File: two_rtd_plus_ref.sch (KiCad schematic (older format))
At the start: 19 parts, among them J3 4-wire RTD, J4 4-wire RTD, J5 Bypass 2nd RTD

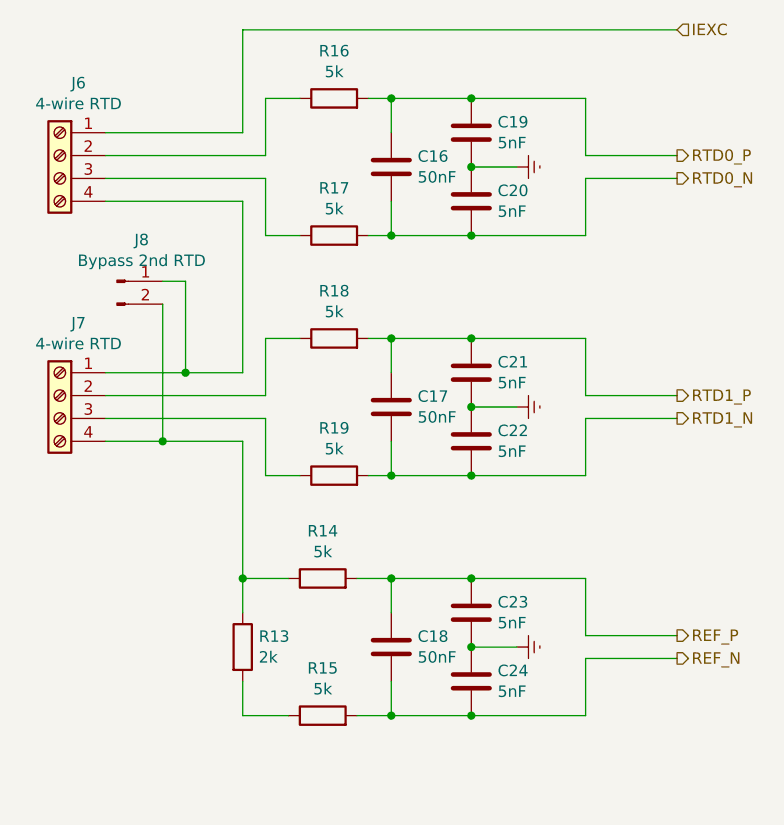
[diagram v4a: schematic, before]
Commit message: placed the components
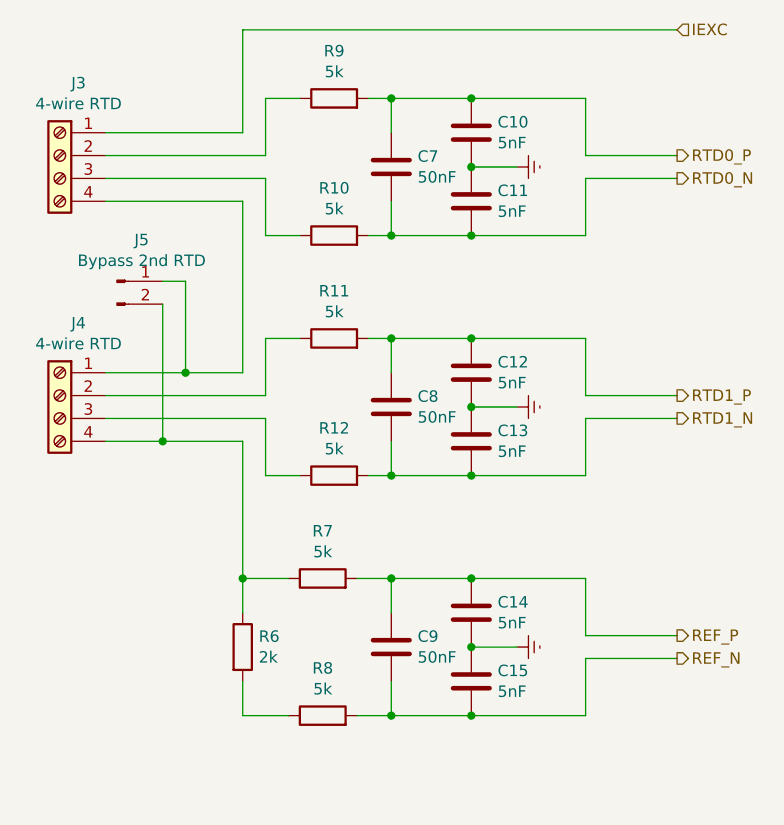
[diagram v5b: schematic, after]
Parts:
- J5: footprint (none) -> Connector_PinHeader_2.54mm:PinHeader_1x02_P2.54mm_Vertical
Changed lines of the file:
@@
 AR Path="/5EC374D6/5EC48F50" Ref="J3"  Part="1"
 AR Path="/5ED0B429/5EC48F50" Ref="J6"  Part="1"
-F 0 "J6" H 3568 2917 50  0000 C CNN
+F 0 "J3" H 3568 2917 50  0000 C CNN
 F 1 "4-wire RTD" H 3568 2826 50  0000 C CNN
 F 2 "temp4x4:screw_term_4x" H 3650 2600 50  0001 C CNN
@@
 AR Path="/5EC374D6/5EC48F56" Ref="C11"  Part="1"
 AR Path="/5ED0B429/5EC48F56" Ref="C20"  Part="1"
-F 0 "C20" H 5565 2846 50  0000 L CNN
+F 0 "C11" H 5565 2846 50  0000 L CNN
 F 1 "5nF" H 5565 2755 50  0000 L CNN
 F 2 "Capacitor_SMD:C_0805_2012Metric_Pad1.15x1.40mm_HandSolder" H 5488 2650 50  0001 C CNN
@@
 AR Path="/5EC374D6/5EC48F5C" Ref="C7"  Part="1"
 AR Path="/5ED0B429/5EC48F5C" Ref="C16"  Part="1"
-F 0 "C16" H 5215 2696 50  0000 L CNN
+F 0 "C7" H 5215 2696 50  0000 L CNN
 F 1 "50nF" H 5215 2605 50  0000 L CNN
 F 2 "Capacitor_SMD:C_0805_2012Metric_Pad1.15x1.40mm_HandSolder" H 5138 2500 50  0001 C CNN
@@
 AR Path="/5EC374D6/5EC48F62" Ref="C10"  Part="1"
 AR Path="/5ED0B429/5EC48F62" Ref="C19"  Part="1"
-F 0 "C19" H 5565 2546 50  0000 L CNN
+F 0 "C10" H 5565 2546 50  0000 L CNN
 F 1 "5nF" H 5565 2455 50  0000 L CNN
 F 2 "Capacitor_SMD:C_0805_2012Metric_Pad1.15x1.40mm_HandSolder" H 5488 2350 50  0001 C CNN
@@
 AR Path="/5EC374D6/5EC48F68" Ref="#PWR014"  Part="1"
 AR Path="/5ED0B429/5EC48F68" Ref="#PWR017"  Part="1"
-F 0 "#PWR017" H 5650 2400 50  0001 C CNN
+F 0 "#PWR014" H 5650 2400 50  0001 C CNN
 F 1 "Earth" H 5650 2500 50  0001 C CNN
 F 2 "" H 5650 2650 50  0001 C CNN
@@
 AR Path="/5EC374D6/5EC48F74" Ref="R9"  Part="1"
 AR Path="/5ED0B429/5EC48F74" Ref="R16"  Part="1"
-F 0 "R16" V 5057 2350 50  0000 C CNN
+F 0 "R9" V 5057 2350 50  0000 C CNN
 F 1 "5k" V 4966 2350 50  0000 C CNN
 F 2 "Resistor_SMD:R_0805_2012Metric_Pad1.15x1.40mm_HandSolder" V 4780 2350 50  0001 C CNN
@@
 AR Path="/5EC374D6/5EC48F7B" Ref="R10"  Part="1"
 AR Path="/5ED0B429/5EC48F7B" Ref="R17"  Part="1"
-F 0 "R17" V 5057 2950 50  0000 C CNN
+F 0 "R10" V 5057 2950 50  0000 C CNN
 F 1 "5k" V 4966 2950 50  0000 C CNN
 F 2 "Resistor_SMD:R_0805_2012Metric_Pad1.15x1.40mm_HandSolder" V 4780 2950 50  0001 C CNN
@@
 AR Path="/5EC374D6/5EC48F91" Ref="J4"  Part="1"
 AR Path="/5ED0B429/5EC48F91" Ref="J7"  Part="1"
-F 0 "J7" H 3568 3967 50  0000 C CNN
+F 0 "J4" H 3568 3967 50  0000 C CNN
 F 1 "4-wire RTD" H 3568 3876 50  0000 C CNN
 F 2 "temp4x4:screw_term_4x" H 3650 3650 50  0001 C CNN
@@
 AR Path="/5EC374D6/5EC48F97" Ref="C13"  Part="1"
 AR Path="/5ED0B429/5EC48F97" Ref="C22"  Part="1"
-F 0 "C22" H 5565 3896 50  0000 L CNN
+F 0 "C13" H 5565 3896 50  0000 L CNN
 F 1 "5nF" H 5565 3805 50  0000 L CNN
 F 2 "Capacitor_SMD:C_0805_2012Metric_Pad1.15x1.40mm_HandSolder" H 5488 3700 50  0001 C CNN
@@
 AR Path="/5EC374D6/5EC48F9D" Ref="C8"  Part="1"
 AR Path="/5ED0B429/5EC48F9D" Ref="C17"  Part="1"
-F 0 "C17" H 5215 3746 50  0000 L CNN
+F 0 "C8" H 5215 3746 50  0000 L CNN
 F 1 "50nF" H 5215 3655 50  0000 L CNN
 F 2 "Capacitor_SMD:C_0805_2012Metric_Pad1.15x1.40mm_HandSolder" H 5138 3550 50  0001 C CNN
@@
 AR Path="/5EC374D6/5EC48FA3" Ref="C12"  Part="1"
 AR Path="/5ED0B429/5EC48FA3" Ref="C21"  Part="1"
-F 0 "C21" H 5565 3596 50  0000 L CNN
+F 0 "C12" H 5565 3596 50  0000 L CNN
 F 1 "5nF" H 5565 3505 50  0000 L CNN
 F 2 "Capacitor_SMD:C_0805_2012Metric_Pad1.15x1.40mm_HandSolder" H 5488 3400 50  0001 C CNN
@@
 AR Path="/5EC374D6/5EC48FA9" Ref="#PWR015"  Part="1"
 AR Path="/5ED0B429/5EC48FA9" Ref="#PWR018"  Part="1"
-F 0 "#PWR018" H 5650 3450 50  0001 C CNN
+F 0 "#PWR015" H 5650 3450 50  0001 C CNN
 F 1 "Earth" H 5650 3550 50  0001 C CNN
 F 2 "" H 5650 3700 50  0001 C CNN
@@
 AR Path="/5EC374D6/5EC48FB5" Ref="R11"  Part="1"
 AR Path="/5ED0B429/5EC48FB5" Ref="R18"  Part="1"
-F 0 "R18" V 5057 3400 50  0000 C CNN
+F 0 "R11" V 5057 3400 50  0000 C CNN
 F 1 "5k" V 4966 3400 50  0000 C CNN
 F 2 "Resistor_SMD:R_0805_2012Metric_Pad1.15x1.40mm_HandSolder" V 4780 3400 50  0001 C CNN
@@
 AR Path="/5EC374D6/5EC48FBC" Ref="R12"  Part="1"
 AR Path="/5ED0B429/5EC48FBC" Ref="R19"  Part="1"
-F 0 "R19" V 5057 4000 50  0000 C CNN
+F 0 "R12" V 5057 4000 50  0000 C CNN
 F 1 "5k" V 4966 4000 50  0000 C CNN
 F 2 "Resistor_SMD:R_0805_2012Metric_Pad1.15x1.40mm_HandSolder" V 4780 4000 50  0001 C CNN
@@
 AR Path="/5EC374D6/5EC48FD1" Ref="C15"  Part="1"
 AR Path="/5ED0B429/5EC48FD1" Ref="C24"  Part="1"
-F 0 "C24" H 5565 4946 50  0000 L CNN
+F 0 "C15" H 5565 4946 50  0000 L CNN
 F 1 "5nF" H 5565 4855 50  0000 L CNN
 F 2 "Capacitor_SMD:C_0805_2012Metric_Pad1.15x1.40mm_HandSolder" H 5488 4750 50  0001 C CNN
@@
 AR Path="/5EC374D6/5EC48FD7" Ref="C9"  Part="1"
 AR Path="/5ED0B429/5EC48FD7" Ref="C18"  Part="1"
-F 0 "C18" H 5215 4796 50  0000 L CNN
+F 0 "C9" H 5215 4796 50  0000 L CNN
 F 1 "50nF" H 5215 4705 50  0000 L CNN
 F 2 "Capacitor_SMD:C_0805_2012Metric_Pad1.15x1.40mm_HandSolder" H 5138 4600 50  0001 C CNN
@@
 AR Path="/5EC374D6/5EC48FDD" Ref="C14"  Part="1"
 AR Path="/5ED0B429/5EC48FDD" Ref="C23"  Part="1"
-F 0 "C23" H 5565 4646 50  0000 L CNN
+F 0 "C14" H 5565 4646 50  0000 L CNN
 F 1 "5nF" H 5565 4555 50  0000 L CNN
 F 2 "Capacitor_SMD:C_0805_2012Metric_Pad1.15x1.40mm_HandSolder" H 5488 4450 50  0001 C CNN
@@
 AR Path="/5EC374D6/5EC48FE3" Ref="#PWR016"  Part="1"
 AR Path="/5ED0B429/5EC48FE3" Ref="#PWR019"  Part="1"
-F 0 "#PWR019" H 5650 4500 50  0001 C CNN
+F 0 "#PWR016" H 5650 4500 50  0001 C CNN
 F 1 "Earth" H 5650 4600 50  0001 C CNN
 F 2 "" H 5650 4750 50  0001 C CNN
@@
 AR Path="/5EC374D6/5EC48FEF" Ref="R7"  Part="1"
 AR Path="/5ED0B429/5EC48FEF" Ref="R14"  Part="1"
-F 0 "R14" V 5007 4450 50  0000 C CNN
+F 0 "R7" V 5007 4450 50  0000 C CNN
 F 1 "5k" V 4916 4450 50  0000 C CNN
 F 2 "Resistor_SMD:R_0805_2012Metric_Pad1.15x1.40mm_HandSolder" V 4730 4450 50  0001 C CNN
@@
 AR Path="/5EC374D6/5EC48FF6" Ref="R8"  Part="1"
 AR Path="/5ED0B429/5EC48FF6" Ref="R15"  Part="1"
-F 0 "R15" V 5007 5050 50  0000 C CNN
+F 0 "R8" V 5007 5050 50  0000 C CNN
 F 1 "5k" V 4916 5050 50  0000 C CNN
 F 2 "Resistor_SMD:R_0805_2012Metric_Pad1.15x1.40mm_HandSolder" V 4730 5050 50  0001 C CNN
@@
 AR Path="/5EC374D6/5EC49006" Ref="R6"  Part="1"
 AR Path="/5ED0B429/5EC49006" Ref="R13"  Part="1"
-F 0 "R13" H 4520 4796 50  0000 L CNN
+F 0 "R6" H 4520 4796 50  0000 L CNN
 F 1 "2k" H 4520 4705 50  0000 L CNN
 F 2 "Resistor_SMD:R_0805_2012Metric_Pad1.15x1.40mm_HandSolder" V 4380 4750 50  0001 C CNN
@@
 AR Path="/5EC374D6/5ECF80D6" Ref="J5"  Part="1"
 AR Path="/5ED0B429/5ECF80D6" Ref="J8"  Part="1"
-F 0 "J8" H 4008 3331 50  0000 C CNN
+F 0 "J5" H 4008 3331 50  0000 C CNN
 F 1 "Bypass 2nd RTD" H 4008 3240 50  0000 C CNN
-F 2 "" H 3900 3150 50  0001 C CNN
+F 2 "Connector_PinHeader_2.54mm:PinHeader_1x02_P2.54mm_Vertical" H 3900 3150 50  0001 C CNN
 F 3 "~" H 3900 3150 50  0001 C CNN
 	1    3900 3150

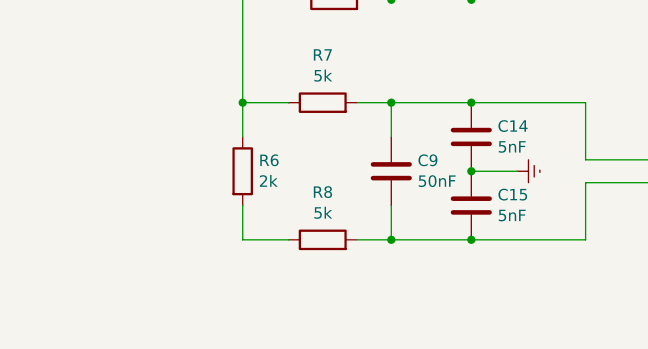
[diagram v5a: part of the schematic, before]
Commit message: changed pin connections to simplify the layout
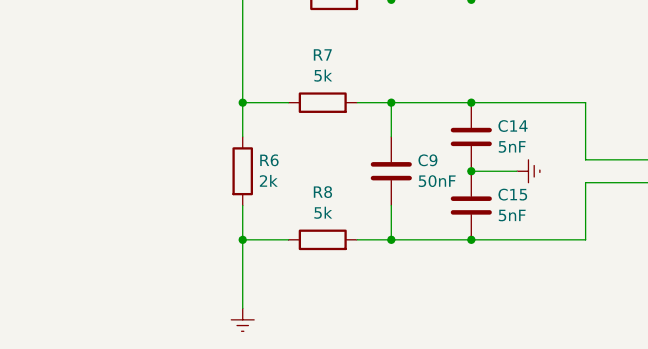
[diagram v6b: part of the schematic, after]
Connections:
- net Earth: now also R6.2, R8.1
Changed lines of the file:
@@
 AR Path="/5EC374D6/5EC48F68" Ref="#PWR014"  Part="1"
 AR Path="/5ED0B429/5EC48F68" Ref="#PWR017"  Part="1"
-F 0 "#PWR014" H 5650 2400 50  0001 C CNN
+F 0 "#PWR017" H 5650 2400 50  0001 C CNN
 F 1 "Earth" H 5650 2500 50  0001 C CNN
 F 2 "" H 5650 2650 50  0001 C CNN
@@
 AR Path="/5EC374D6/5EC48FA9" Ref="#PWR015"  Part="1"
 AR Path="/5ED0B429/5EC48FA9" Ref="#PWR018"  Part="1"
-F 0 "#PWR015" H 5650 3450 50  0001 C CNN
+F 0 "#PWR018" H 5650 3450 50  0001 C CNN
 F 1 "Earth" H 5650 3550 50  0001 C CNN
 F 2 "" H 5650 3700 50  0001 C CNN
@@
 AR Path="/5EC374D6/5EC48FE3" Ref="#PWR016"  Part="1"
 AR Path="/5ED0B429/5EC48FE3" Ref="#PWR019"  Part="1"
-F 0 "#PWR016" H 5650 4500 50  0001 C CNN
+F 0 "#PWR019" H 5650 4500 50  0001 C CNN
 F 1 "Earth" H 5650 4600 50  0001 C CNN
 F 2 "" H 5650 4750 50  0001 C CNN
@@
 Wire Wire Line
 	4100 3850 4450 3850
+$Comp
+L power:Earth #PWR0101
+U 1 1 5ED21BBD
+P 4450 5350
+AR Path="/5EC374D6/5ED21BBD" Ref="#PWR0101"  Part="1"
+AR Path="/5ED0B429/5ED21BBD" Ref="#PWR0102"  Part="1"
+F 0 "#PWR0102" H 4450 5100 50  0001 C CNN
+F 1 "Earth" H 4450 5200 50  0001 C CNN
+F 2 "" H 4450 5350 50  0001 C CNN
+F 3 "~" H 4450 5350 50  0001 C CNN
+	1    4450 5350
+	1    0    0    -1
+$EndComp
+Wire Wire Line
+	4450 5050 4450 5350
+Connection ~ 4450 5050
 $EndSCHEMATC
